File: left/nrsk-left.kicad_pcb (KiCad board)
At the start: 2 copper layers, 163.2 x 120.3 mm, 119 parts, among them J1 PJ-320D, J2 USB-C, SW1 Esc, SW10 1, SW11 2, SW12 3, SW13 4, SW14 5, SW15 6, SW16 16, SW17 Tab, SW18 Q, SW19 W, SW2 F1, SW20 E, SW21 R, SW22 T, SW23 23, SW24 Ctrl, SW25 A, SW26 S, SW27 D, SW28 F, SW29 G, SW3 F2, SW30 30, SW31 Shift, SW32 Z, SW33 X, SW34 C, SW35 V, SW36 B, SW37 37, SW38 Ctrl, SW39 Opt, SW4 F3, SW40 Cmd, SW41 Space, SW42 Space, SW43 Space, SW44 44, SW5 F4, SW6 F5, SW7 F6, SW8 8, SW9 `, U1 ATmega32U4-AU, U2 USBLC6-2SC6, Y1 16MHz

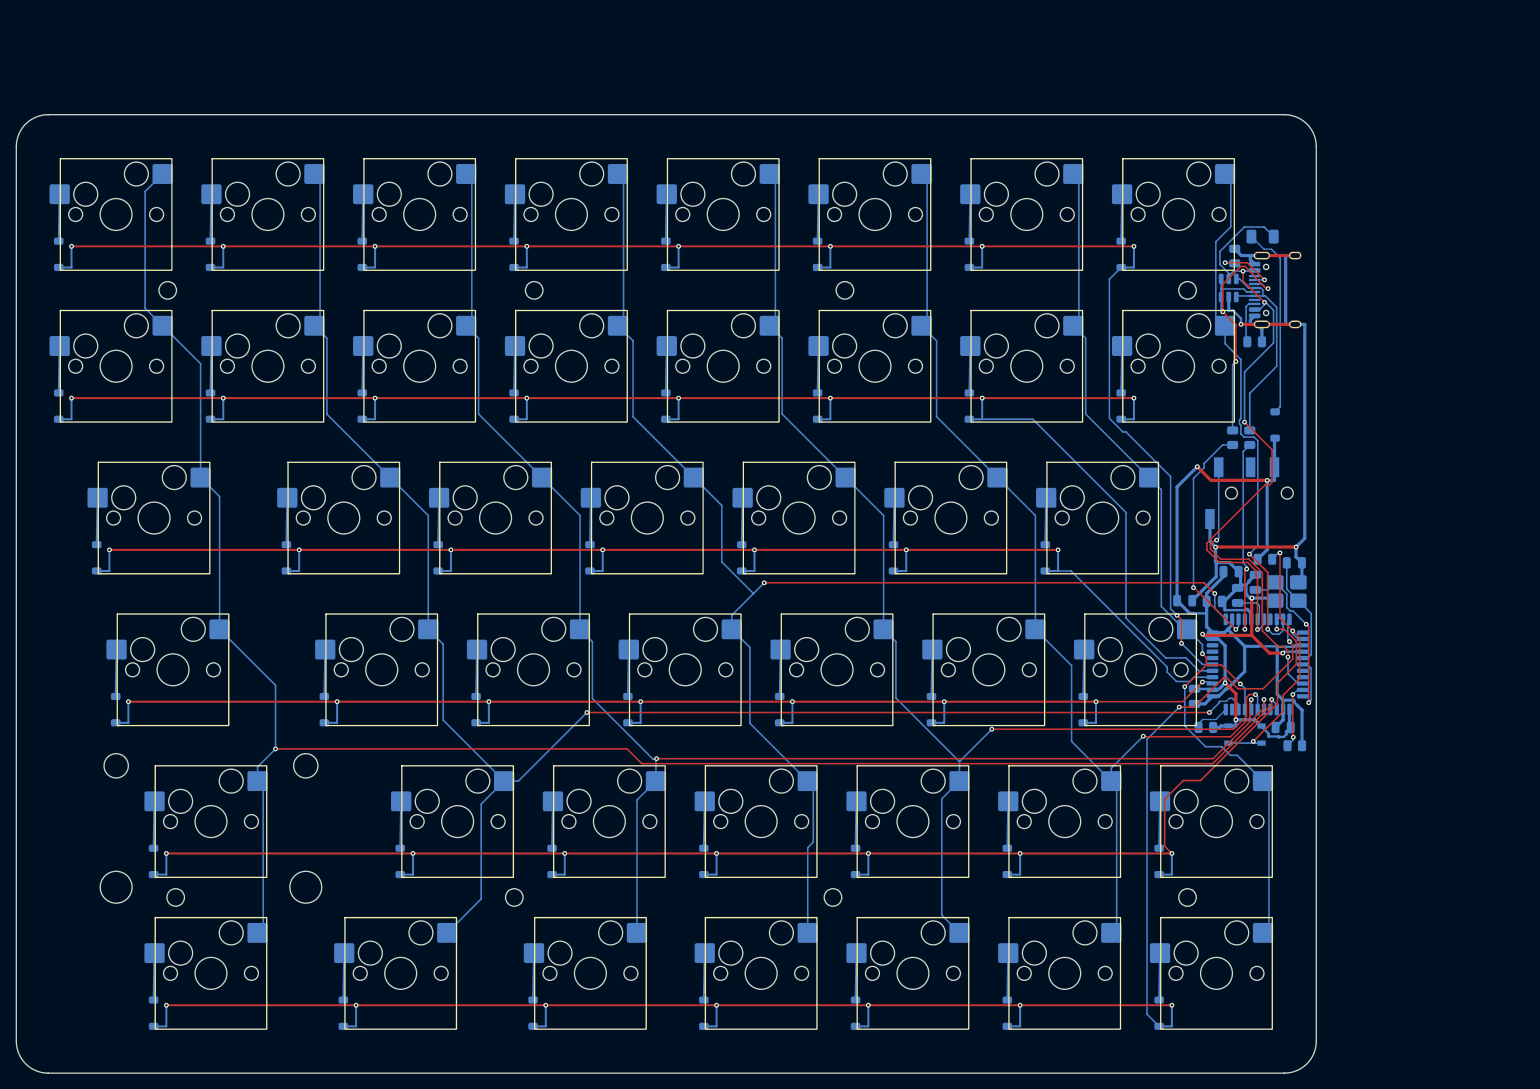
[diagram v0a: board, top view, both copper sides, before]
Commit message: Add OLED displays, OLED placement study and high-resolution renders
- 0.91" 128x32 SSD1306 OLED on both halves (I2C on PD0/PD1, 4.7k pull-ups),
  placed in the key-free inner notch; boards re-routed, ERC/DRC clean
- Switch plate window with a 2 mm clear acrylic cover lying on the plate,
  shaped around the switch tops; keyboard height unchanged
- QMK: OLED enabled (layer/caps on the master, WPM on the other half),
  split sync of layer, LED state and WPM
- BOM: OLED modules, pull-ups, cover acrylic and screws
- OLED height/tilt study: flush, 3.5/6.5/13 mm pods and two tilted pods,
  checked clear of keycaps and inside the case outline
- Blender renders at 2400 px and a grouped, numbered overview sheet

Co-Authored-By: Claude Opus 5.5 <noreply@anthropic.com>
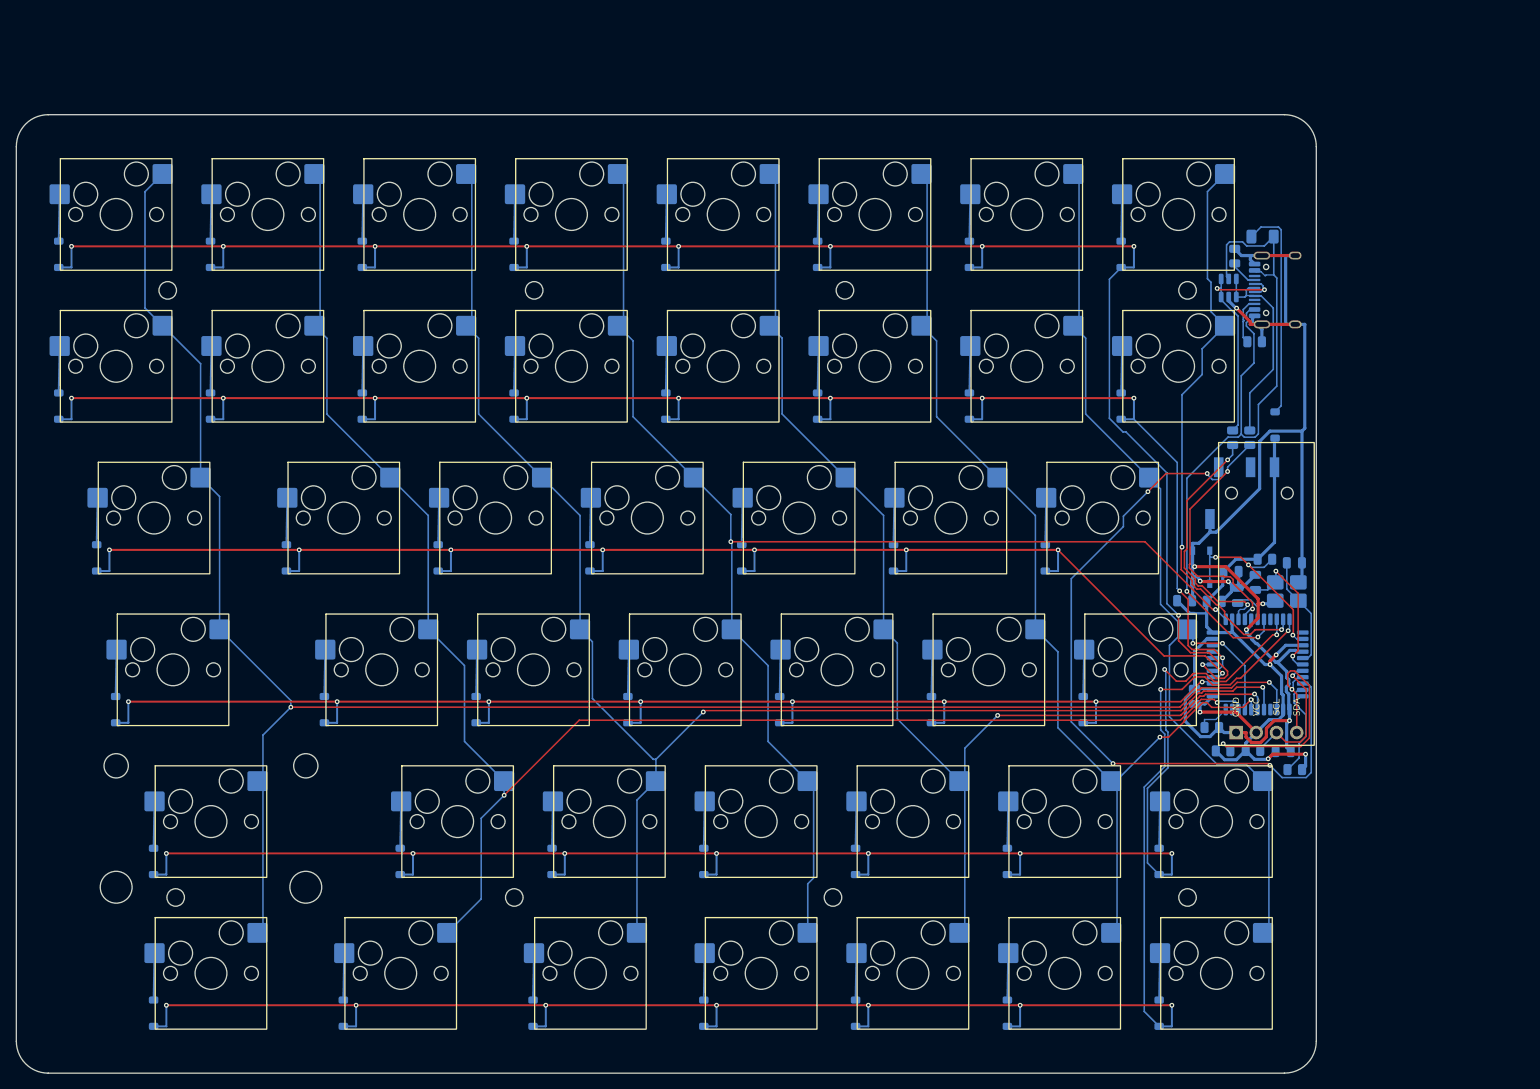
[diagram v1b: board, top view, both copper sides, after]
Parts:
- added J3: OLED 128x32, nrsk:OLED_0.91in_128x32_I2C, F.Cu at (183.9, 87.2)
- added R8: 4.7k, Resistor_SMD:R_0805_2012Metric, B.Cu at (182.2, 106.8)
- added R9: 4.7k, Resistor_SMD:R_0805_2012Metric, B.Cu at (178.5, 106.8)
- moved RSW1 21.7 mm to (175.7, 83.8), turned to 90 degrees
- moved C6 3.00 mm to (186.0, 106.9)
- moved R1 3.00 mm to (187.5, 109.2)
- moved R7 0.75 mm to (177.1, 103.9)
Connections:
- U1 pad 18: unconnected-(U1-PD0-Pad18) -> /SCL
- U1 pad 19: unconnected-(U1-PD1-Pad19) -> /SDA
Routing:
- net /DATA: track 35.3 -> 89.9 mm, vias 2 -> 4
- net /SDA: track 0.00 -> 33.1 mm, vias 0 -> 2
- net GND: track 165.1 -> 187.4 mm, vias 8 -> 7
- net /VBUS: track 77.3 -> 97.1 mm, vias 4 -> 2
- net /SCL: track 0.00 -> 17.4 mm, vias 0 -> 1
- net /ROW1: track 217.1 -> 206.1 mm, vias 8 -> 10
- net /RST: track 34.8 -> 25.5 mm
- net VCC: track 100.6 -> 92.4 mm, vias 2 -> 5
- net /ROW4: track 195.4 -> 203.4 mm, vias 8 -> 9
- net /ROW0: track 224.1 -> 232.1 mm
- net /USB_D-: track 37.5 -> 29.7 mm, vias 3 -> 2
- net /XTAL1: track 25.6 -> 18.4 mm
- net /COL6: track 119.2 -> 125.6 mm, vias 3 -> 2
- net /D+: track 25.0 -> 31.2 mm
- net /COL7: track 66.4 -> 71.9 mm
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
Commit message: Match both halves' size, align TRRS jacks, document firmware flashing
- Left board widened on its inner side to the right board's outline
  (both 187.0 x 120.3 mm, cases 204.0 x 137.3 mm); MCU, USB-C, TRRS and
  OLED placed as a mirror of the right half
- TRRS jacks at the same height on both halves (109 mm from the top),
  USB-C likewise (81 mm)
- Router cleanup removes dangling track stubs left by Freerouting
- README: step-by-step QMK build and DFU flashing for each half,
  troubleshooting and ISP recovery
- Renders and OLED study regenerated for the new layout

Co-Authored-By: Claude Opus 5.5 <noreply@anthropic.com>
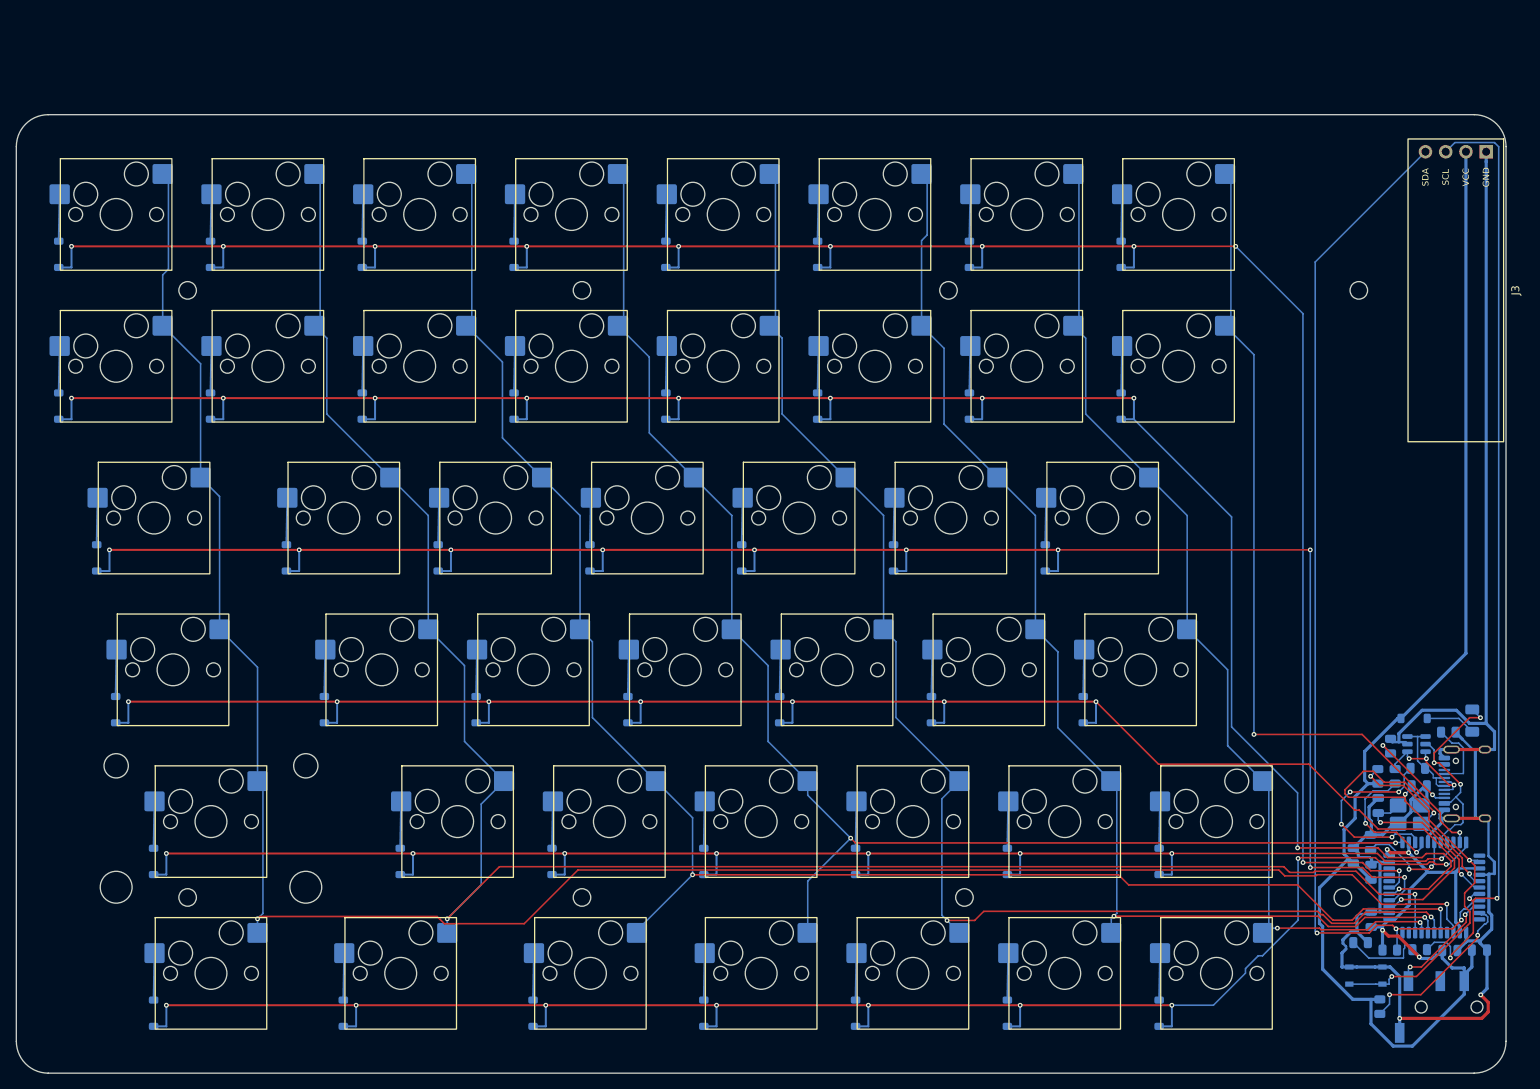
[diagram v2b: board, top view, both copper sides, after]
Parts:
- moved J1 68.8 mm to (205.6, 139.0)
- moved J2 66.4 mm to (210.3, 111.0)
- moved F1 66.2 mm to (209.7, 103.0), turned to 90 degrees
- moved R4 65.5 mm to (206.7, 104.5), turned to 0 degrees
- moved U2 61.9 mm to (202.7, 106.0), turned to 0 degrees
- moved C5 56.8 mm to (210.6, 131.8)
- moved RSW1 55.3 mm to (196.4, 135.1), turned to 0 degrees
- moved R5 53.5 mm to (199.5, 106.2), turned to 90 degrees
- moved R3 47.6 mm to (202.9, 109.0), turned to 0 degrees
- moved R2 46.3 mm to (200.1, 110.0)
- moved J3 44.9 mm to (207.7, 49.0), turned to -90 degrees
- moved D99 40.7 mm to (202.4, 102.8), turned to 0 degrees
- moved C4 39.3 mm to (197.0, 122.1), turned to 90 degrees
- moved C7 38.4 mm to (194.8, 120.0), turned to 90 degrees
- moved C8 35.7 mm to (197.1, 128.0)
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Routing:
- net VCC: track 92.4 -> 202.4 mm, vias 5 -> 4
- net /SCL: track 17.4 -> 120.3 mm, vias 1 -> 3
- net /SDA: track 33.1 -> 129.8 mm, vias 2 -> 3
- net /DATA: track 89.9 -> 14.4 mm, vias 4 -> 2
- net /VBUS: track 97.1 -> 30.5 mm, vias 2 -> 3
- net /ROW2: track 177.3 -> 236.8 mm, vias 8 -> 10
- net /ROW1: track 206.1 -> 259.9 mm
- net /ROW3: track 166.9 -> 215.6 mm
- net GND: track 187.4 -> 232.5 mm, vias 7 -> 2
- net /ROW0: track 232.1 -> 276.4 mm, vias 10 -> 11
- net /COL7: track 71.9 -> 105.2 mm
- net /COL1: track 206.8 -> 239.2 mm
- net /XTAL2: track 14.0 -> 41.2 mm, vias 0 -> 3
- net /COL0: track 234.1 -> 259.8 mm
- net /RST: track 25.5 -> 47.6 mm
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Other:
- board size 163.2 x 120.3 mm -> 187 x 120.3 mm

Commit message: Add corner thumbwheels read by AS5600, preview-quality renders
- Thumbwheel (29.2 mm, knurled) at the left half's top-left and the right
  half's top-right corner, lying under the PCB with its rim out of the
  corner; read contact-free by an AS5600 on the PCB back through a
  diametric magnet, on the existing I2C bus (no extra pins)
- Left Esc switch turned 180 deg so its socket clears the sensor
- Case: wall opening at the corner, axle post (print) / M3 axle (acrylic),
  corner screws moved beside the opening, printable wheel STL
- QMK: nrsk.c polls the sensor and forwards the other half's steps over a
  split RPC; dial_update_user() in the keymap (volume / page by default)
- Router cleanup runs in a separate process (reloading a board in the
  same process returned a broken object and stopped the build)
- Renders default to a quick preview (1200 px); FINAL=1 for 2400 px
- Side dial comparison renders kept in docs/img/dial-study

Co-Authored-By: Claude Opus 5.5 <noreply@anthropic.com>
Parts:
- added C10: 0.1uF, Capacitor_SMD:C_0805_2012Metric, B.Cu at (33.5, 35.9)
- added C9: 1uF, Capacitor_SMD:C_0805_2012Metric, B.Cu at (29.8, 35.9)
- added U3: AS5600-ASOM, Package_SO:SOIC-8_3.9x4.9mm_P1.27mm, B.Cu at (32.0, 32.0)
- moved D1 17.5 mm to (46.7, 34.5), turned to -90 degrees
- turned SW1 to 180 degrees
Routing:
- net /SCL: track 120.3 -> 309.9 mm
- net GND: track 232.5 -> 421.1 mm, vias 2 -> 5
- net /SDA: track 129.8 -> 296.9 mm, vias 3 -> 6
- net VCC: track 202.4 -> 362.9 mm, vias 4 -> 6
- net /XTAL2: track 41.2 -> 20.0 mm, vias 3 -> 2
- net /ROW1: track 259.9 -> 244.0 mm
- net /ROW0: track 276.4 -> 261.2 mm, vias 11 -> 9
- net /RST: track 47.6 -> 57.4 mm
- net /ROW2: track 236.8 -> 227.1 mm
- net /D-: track 25.0 -> 17.1 mm, vias 4 -> 2
- net /COL7: track 105.2 -> 111.2 mm
- net /COL1: track 239.2 -> 233.6 mm
- net /D+: track 17.1 -> 11.7 mm
- net /COL0: track 259.8 -> 254.8 mm
- net /CC1: track 9.26 -> 14.0 mm, vias 0 -> 2
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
